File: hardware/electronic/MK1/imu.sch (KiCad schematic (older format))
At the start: 8 parts

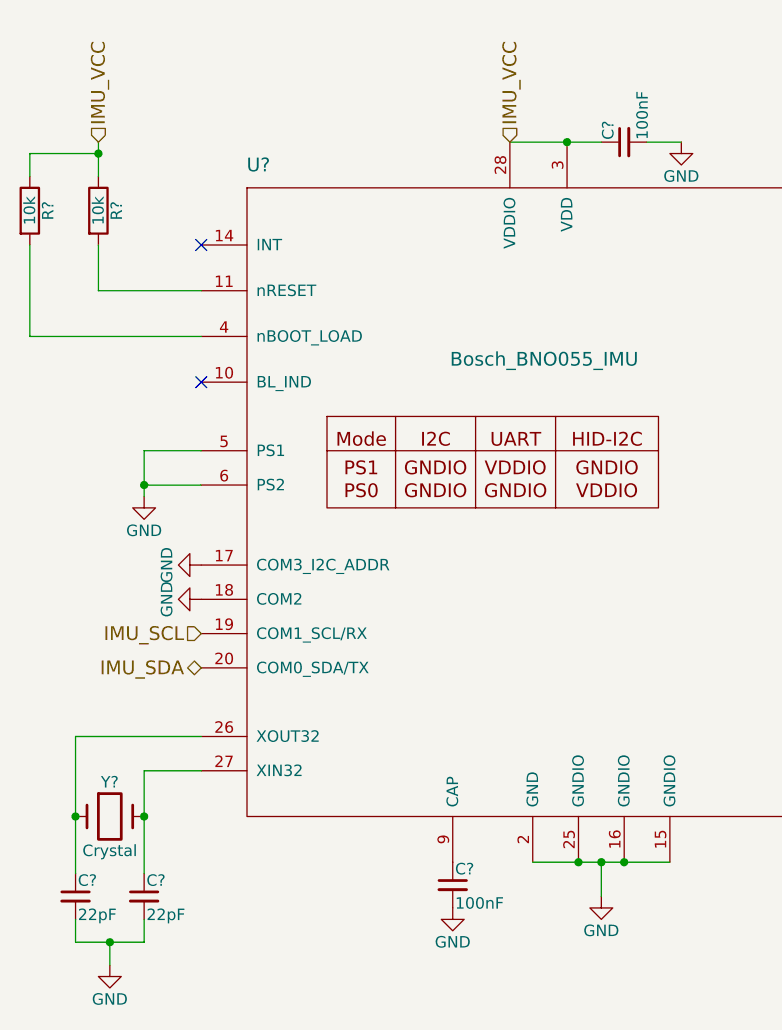
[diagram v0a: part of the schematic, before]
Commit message: HW: Add the IMU to the PCB layout
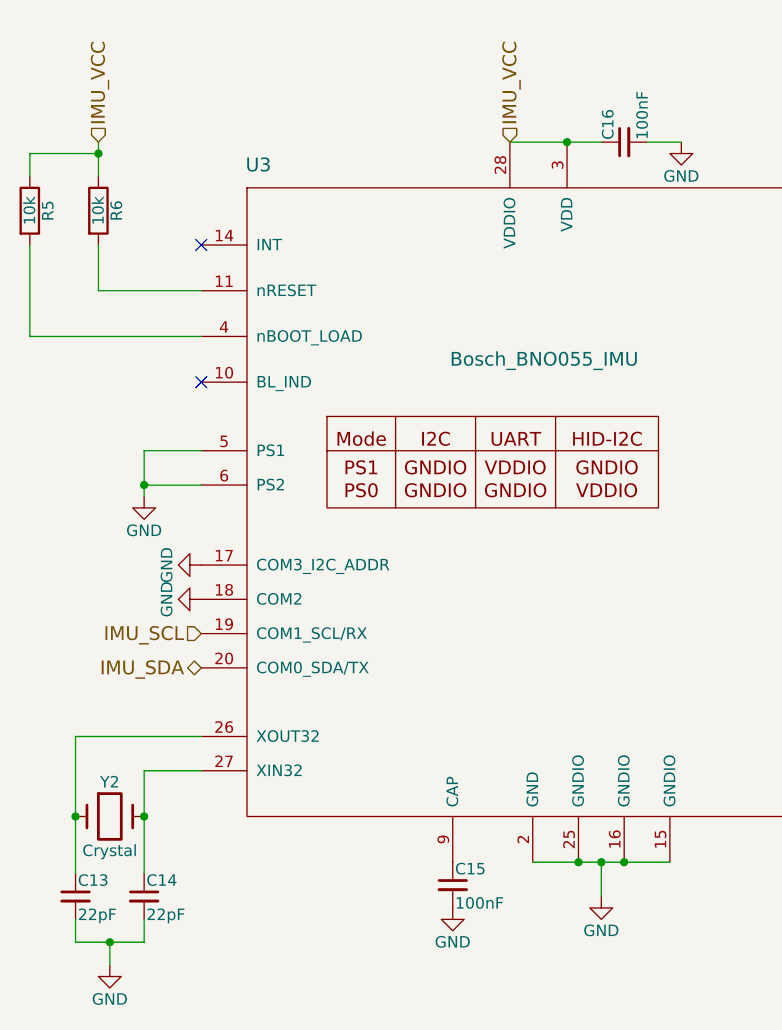
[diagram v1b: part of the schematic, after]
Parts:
- C13, C14, C15, C16: renamed from C?; footprint (none) -> Capacitors_SMD:C_0805
- R5, R6: renamed from R?; footprint (none) -> Resistors_SMD:R_0805
- U3: renamed from U?; footprint (none) -> OPAVES_Footprints:LGA-28
- Y2: renamed from Y?; footprint (none) -> Crystals:Crystal_HC50-U_Vertical
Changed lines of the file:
@@
 $EndDescr
 $Comp
-L Bosch_BNO055_IMU U?
+L Bosch_BNO055_IMU U3
 U 1 1 5886EE63
 P 4350 2100
-F 0 "U?" H 4400 2200 60  0000 C CNN
+F 0 "U3" H 4400 2200 60  0000 C CNN
 F 1 "Bosch_BNO055_IMU" H 5650 1350 60  0000 C CNN
-F 2 "" H 4350 2100 60  0001 C CNN
+F 2 "OPAVES_Footprints:LGA-28" H 4350 2100 60  0001 C CNN
 F 3 "" H 4350 2100 60  0001 C CNN
 	1    4350 2100
@@
 $EndComp
 $Comp
-L C_Small C?
+L C_Small C15
 U 1 1 5886EF60
 P 5250 5150
-F 0 "C?" H 5260 5220 50  0000 L CNN
+F 0 "C15" H 5260 5220 50  0000 L CNN
 F 1 "100nF" H 5260 5070 50  0000 L CNN
-F 2 "" H 5250 5150 50  0000 C CNN
+F 2 "Capacitors_SMD:C_0805" H 5250 5150 50  0001 C CNN
 F 3 "" H 5250 5150 50  0000 C CNN
 	1    5250 5150
@@
 $EndComp
 $Comp
-L GND #PWR?
+L GND #PWR010
 U 1 1 5886F001
 P 5250 5250
-F 0 "#PWR?" H 5250 5000 50  0001 C CNN
+F 0 "#PWR010" H 5250 5000 50  0001 C CNN
 F 1 "GND" H 5250 5100 50  0000 C CNN
 F 2 "" H 5250 5250 50  0000 C CNN
@@
 Connection ~ 5900 5050
 $Comp
-L GND #PWR?
+L GND #PWR011
 U 1 1 5886F07C
 P 5900 5200
-F 0 "#PWR?" H 5900 4950 50  0001 C CNN
+F 0 "#PWR011" H 5900 4950 50  0001 C CNN
 F 1 "GND" H 5900 5050 50  0000 C CNN
 F 2 "" H 5900 5200 50  0000 C CNN
@@
 Connection ~ 3900 3400
 $Comp
-L GND #PWR?
+L GND #PWR012
 U 1 1 5886F184
 P 3900 3450
-F 0 "#PWR?" H 3900 3200 50  0001 C CNN
+F 0 "#PWR012" H 3900 3200 50  0001 C CNN
 F 1 "GND" H 3900 3300 50  0000 C CNN
 F 2 "" H 3900 3450 50  0000 C CNN
@@
 	5500 1900 5900 1900
 $Comp
-L C_Small C?
+L C_Small C16
 U 1 1 5886F317
 P 6000 1900
-F 0 "C?" H 6010 1970 50  0000 L CNN
+F 0 "C16" H 6010 1970 50  0000 L CNN
 F 1 "100nF" H 6010 1820 50  0000 L CNN
-F 2 "" H 6000 1900 50  0000 C CNN
+F 2 "Capacitors_SMD:C_0805" H 6000 1900 50  0001 C CNN
 F 3 "" H 6000 1900 50  0000 C CNN
 	1    6000 1900
@@
 $EndComp
 $Comp
-L GND #PWR?
+L GND #PWR013
 U 1 1 5886F3DB
 P 6250 1900
-F 0 "#PWR?" H 6250 1650 50  0001 C CNN
+F 0 "#PWR013" H 6250 1650 50  0001 C CNN
 F 1 "GND" H 6250 1750 50  0000 C CNN
 F 2 "" H 6250 1900 50  0000 C CNN
@@
 	6100 1900 6250 1900
 $Comp
-L Crystal Y?
+L Crystal Y2
 U 1 1 5886F6E7
 P 3750 4850
-F 0 "Y?" H 3750 5000 50  0000 C CNN
+F 0 "Y2" H 3750 5000 50  0000 C CNN
 F 1 "Crystal" H 3750 4700 50  0000 C CNN
-F 2 "" H 3750 4850 50  0000 C CNN
+F 2 "Crystals:Crystal_HC50-U_Vertical" H 3750 4850 50  0001 C CNN
 F 3 "" H 3750 4850 50  0000 C CNN
 	1    3750 4850
@@
 	3900 4650 3900 5100
 $Comp
-L C_Small C?
+L C_Small C13
 U 1 1 5886F76D
 P 3600 5200
-F 0 "C?" H 3610 5270 50  0000 L CNN
+F 0 "C13" H 3610 5270 50  0000 L CNN
 F 1 "22pF" H 3610 5120 50  0000 L CNN
-F 2 "" H 3600 5200 50  0000 C CNN
+F 2 "Capacitors_SMD:C_0805" H 3600 5200 50  0001 C CNN
 F 3 "" H 3600 5200 50  0000 C CNN
 	1    3600 5200
@@
 $EndComp
 $Comp
-L C_Small C?
+L C_Small C14
 U 1 1 5886F80E
 P 3900 5200
-F 0 "C?" H 3910 5270 50  0000 L CNN
+F 0 "C14" H 3910 5270 50  0000 L CNN
 F 1 "22pF" H 3910 5120 50  0000 L CNN
-F 2 "" H 3900 5200 50  0000 C CNN
+F 2 "Capacitors_SMD:C_0805" H 3900 5200 50  0001 C CNN
 F 3 "" H 3900 5200 50  0000 C CNN
 	1    3900 5200
@@
 Connection ~ 3750 5400
 $Comp
-L GND #PWR?
+L GND #PWR014
 U 1 1 5886F8B7
 P 3750 5500
-F 0 "#PWR?" H 3750 5250 50  0001 C CNN
+F 0 "#PWR014" H 3750 5250 50  0001 C CNN
 F 1 "GND" H 3750 5350 50  0000 C CNN
 F 2 "" H 3750 5500 50  0000 C CNN
@@
 $EndComp
 $Comp
-L GND #PWR?
+L GND #PWR015
 U 1 1 5886FCA1
 P 4150 3900
-F 0 "#PWR?" H 4150 3650 50  0001 C CNN
+F 0 "#PWR015" H 4150 3650 50  0001 C CNN
 F 1 "GND" H 4150 3750 50  0000 C CNN
 F 2 "" H 4150 3900 50  0000 C CNN
@@
 $EndComp
 $Comp
-L R R?
+L R R6
 U 1 1 5886FDF0
 P 3700 2200
-F 0 "R?" V 3780 2200 50  0000 C CNN
+F 0 "R6" V 3780 2200 50  0000 C CNN
 F 1 "10k" V 3700 2200 50  0000 C CNN
-F 2 "" V 3630 2200 50  0000 C CNN
+F 2 "Resistors_SMD:R_0805" V 3630 2200 50  0001 C CNN
 F 3 "" H 3700 2200 50  0000 C CNN
 	1    3700 2200
@@
 	3700 2050 3700 1900
 $Comp
-L R R?
+L R R5
 U 1 1 588701AF
 P 3400 2200
-F 0 "R?" V 3480 2200 50  0000 C CNN
+F 0 "R5" V 3480 2200 50  0000 C CNN
 F 1 "10k" V 3400 2200 50  0000 C CNN
-F 2 "" V 3330 2200 50  0000 C CNN
+F 2 "Resistors_SMD:R_0805" V 3330 2200 50  0001 C CNN
 F 3 "" H 3400 2200 50  0000 C CNN
 	1    3400 2200
@@
 	3400 2750 3400 2350
 $Comp
-L GND #PWR?
+L GND #PWR016
 U 1 1 58870499
 P 4150 3750
-F 0 "#PWR?" H 4150 3500 50  0001 C CNN
+F 0 "#PWR016" H 4150 3500 50  0001 C CNN
 F 1 "GND" H 4150 3600 50  0000 C CNN
 F 2 "" H 4150 3750 50  0000 C CNN

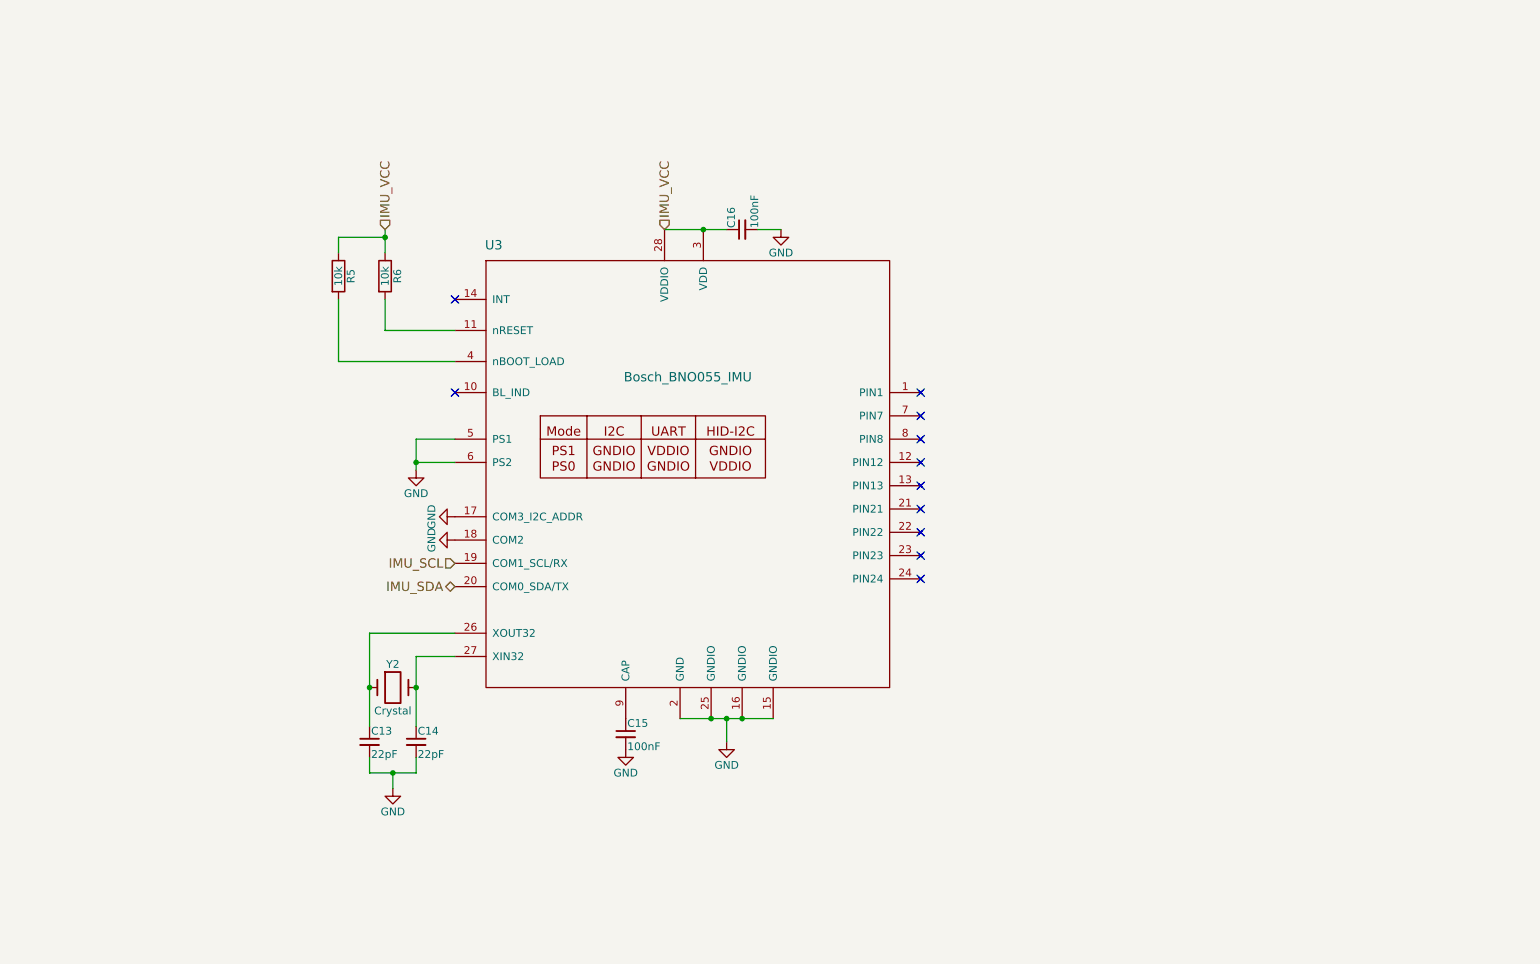
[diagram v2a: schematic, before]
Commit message: HW: Add an AdaFruit BNO055 breakout backup for the IMU
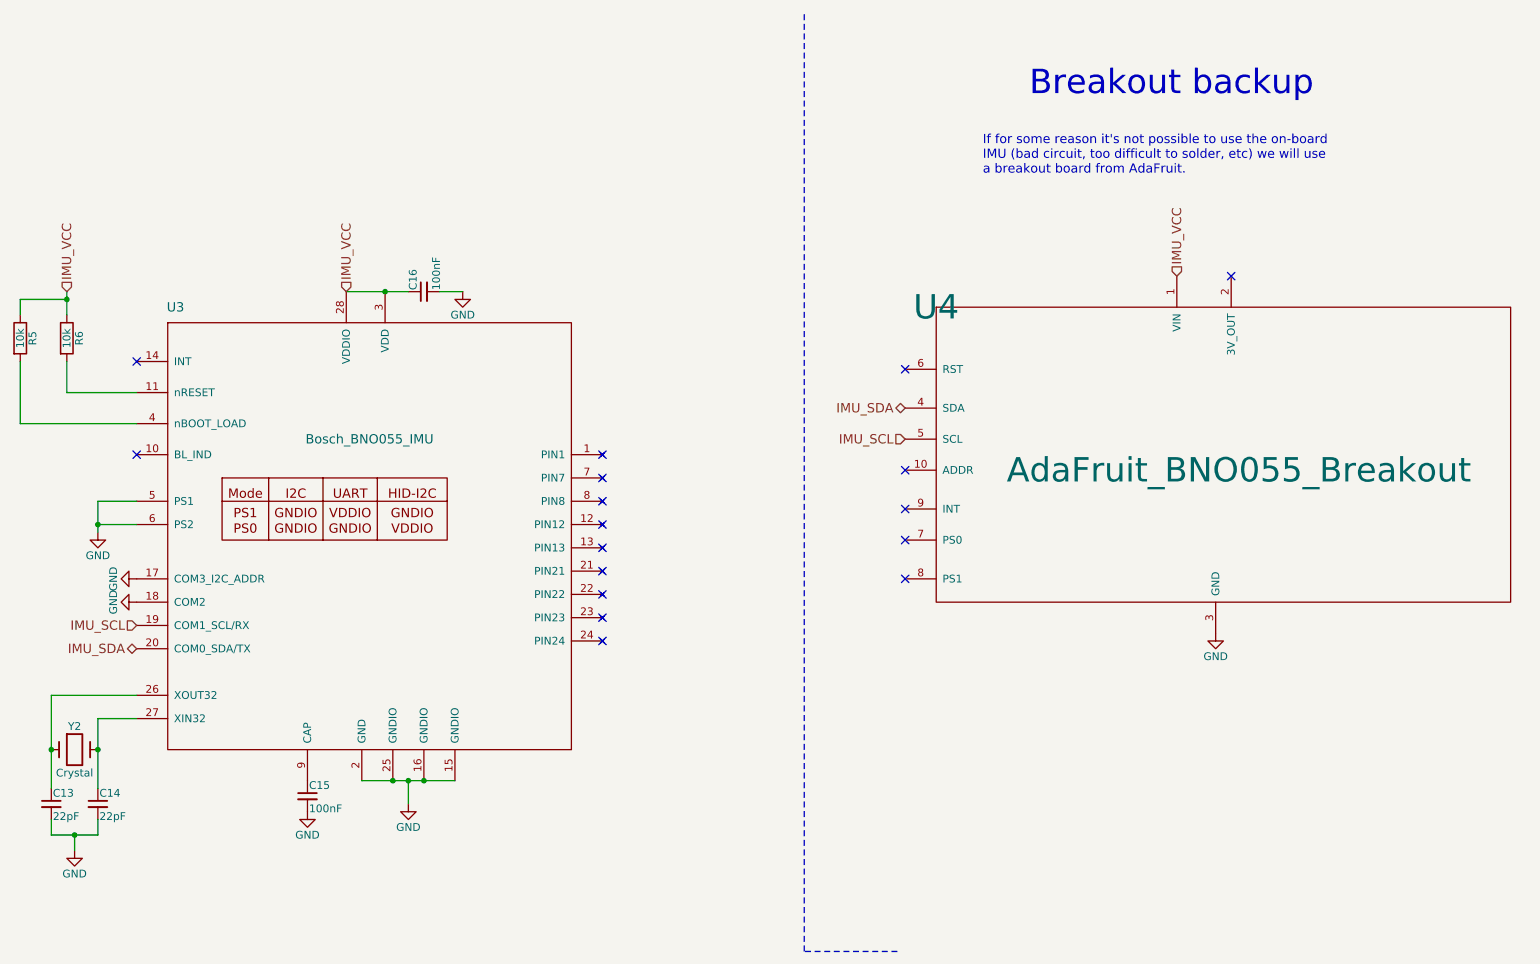
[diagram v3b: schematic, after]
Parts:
- added U4: AdaFruit_BNO055_Breakout, OPAVES_Footprints:AdaFruit_BNO055_Breakout, symbol AdaFruit_BNO055_Breakout
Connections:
- net GND: now also U4.3 (GND)
- net IMU_SCL: now also U4.5 (SCL)
- net IMU_SDA: now also U4.4 (SDA)
- net IMU_VCC: now also U4.1 (VIN)
- no-connect marks 11 -> 17
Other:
- note added: "Breakout backup"
- note added: "If for some reason it's not possible to use the on-board \nIMU (bad circuit, too difficult to solder, etc) we will use \na breakout board from AdaFruit."
- moved on the sheet: C13, C14, C15, C16, R5, R6, U3, Y2
